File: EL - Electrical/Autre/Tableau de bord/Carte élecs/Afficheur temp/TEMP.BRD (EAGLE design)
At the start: 82 x 40 mm, 24 parts, among them IC1 MCP23008P, IC2 MCP23008P, X1 22-23-2041

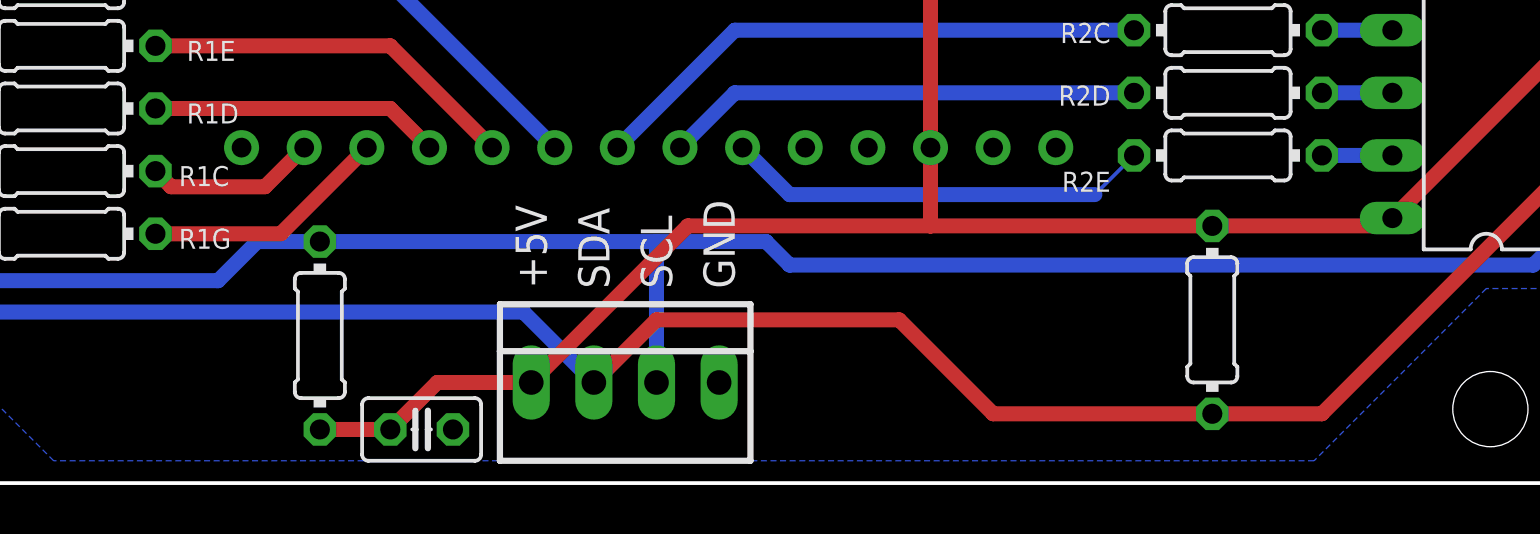
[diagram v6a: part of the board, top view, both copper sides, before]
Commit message: ajout listes composants
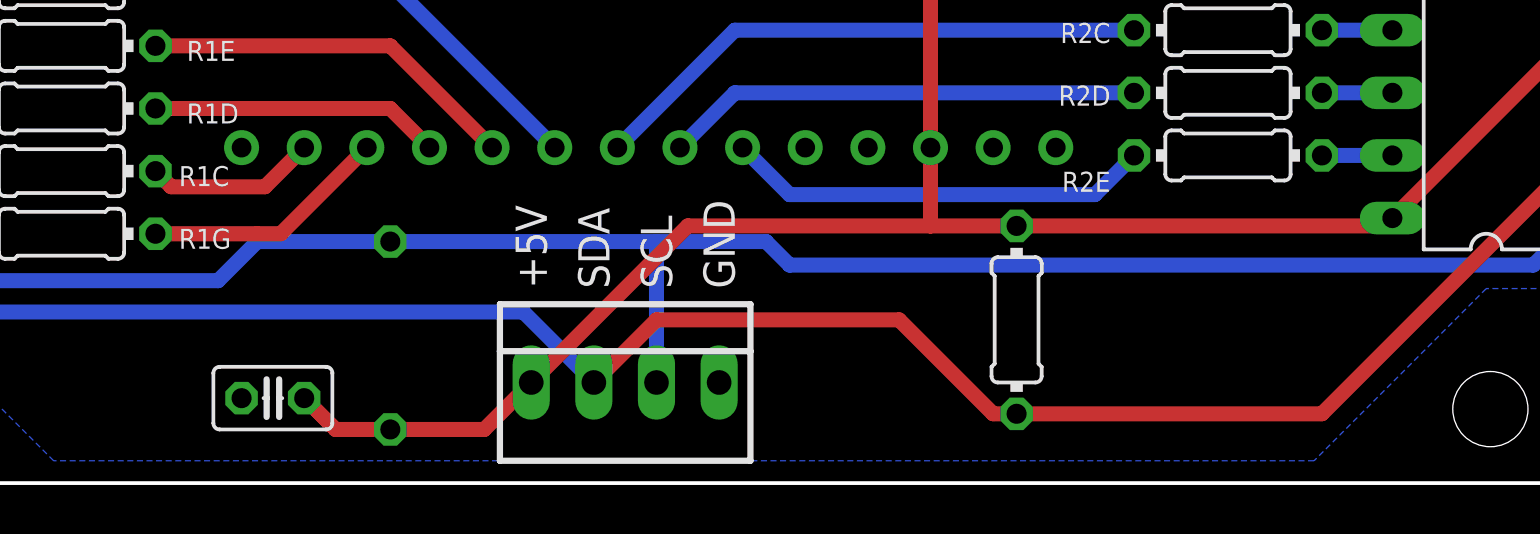
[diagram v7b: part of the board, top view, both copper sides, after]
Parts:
- moved R2 7.94 mm to (57.8, 7.62)
- moved C1 6.16 mm to (27.6, 4.45), turned to 180 degrees
- moved R1 2.86 mm to (32.4, 6.99), flipped to the bottom
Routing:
- net +5V: track 142.5 -> 143.7 mm
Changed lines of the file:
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@@
 </autorouter>
 <elements>
-<element name="C1" library="rcl" library_urn="urn:adsk.eagle:library:334" package="C025-025X050" package3d_urn="urn:adsk.eagle:package:23629/2" value="500pF" x="33.655" y="3.175" smashed="yes">
-<attribute name="SPICEPREFIX" value="C" x="33.655" y="3.175" size="1.778" layer="27" display="off"/>
-<attribute name="VALUE" x="31.369" y="4.826" size="1.27" layer="27" ratio="10"/>
+<element name="C1" library="rcl" library_urn="urn:adsk.eagle:library:334" package="C025-025X050" package3d_urn="urn:adsk.eagle:package:23629/2" value="500pF" x="27.6225" y="4.445" smashed="yes" rot="R180">
+<attribute name="SPICEPREFIX" value="C" x="27.6225" y="4.445" size="1.778" layer="27" rot="R180" display="off"/>
+<attribute name="VALUE" x="29.9085" y="7.5565" size="1.27" layer="27" ratio="10" rot="R180"/>
 </element>
 <element name="IC1" library="microchip-dspic" package="DIL18" value="MCP23008P" x="76.835" y="21.9075" smashed="yes" rot="R90">
 <attribute name="VALUE" x="77.724" y="11.7475" size="1.778" layer="27" ratio="10" rot="R90"/>
 </element>
-<element name="R1" library="rcl" library_urn="urn:adsk.eagle:library:334" package="0204/7" package3d_urn="urn:adsk.eagle:package:23498/1" value="1k" x="29.5275" y="6.985" smashed="yes" rot="R270">
-<attribute name="SPICEPREFIX" value="R" x="29.5275" y="6.985" size="1.778" layer="27" rot="R270" display="off"/>
-<attribute name="VALUE" x="29.0449" y="8.6106" size="0.9906" layer="27" ratio="10" rot="R270"/>
-</element>
-<element name="R2" library="rcl" library_urn="urn:adsk.eagle:library:334" package="0204/7" package3d_urn="urn:adsk.eagle:package:23498/1" value="1k" x="65.7225" y="7.62" smashed="yes" rot="R270">
-<attribute name="SPICEPREFIX" value="R" x="65.7225" y="7.62" size="1.778" layer="27" rot="R270" display="off"/>
-<attribute name="VALUE" x="65.2399" y="9.2456" size="0.9906" layer="27" ratio="10" rot="R270"/>
+<element name="R1" library="rcl" library_urn="urn:adsk.eagle:library:334" package="0204/7" package3d_urn="urn:adsk.eagle:package:23498/1" value="1k" x="32.385" y="6.985" smashed="yes" rot="MR270">
+<attribute name="SPICEPREFIX" value="R" x="32.385" y="6.985" size="1.778" layer="28" rot="MR270" display="off"/>
+<attribute name="VALUE" x="32.8676" y="8.6106" size="0.9906" layer="28" ratio="10" rot="MR270"/>
+</element>
+<element name="R2" library="rcl" library_urn="urn:adsk.eagle:library:334" package="0204/7" package3d_urn="urn:adsk.eagle:package:23498/1" value="1k" x="57.785" y="7.62" smashed="yes" rot="R270">
+<attribute name="SPICEPREFIX" value="R" x="57.785" y="7.62" size="1.778" layer="27" rot="R270" display="off"/>
+<attribute name="VALUE" x="57.3024" y="9.2456" size="0.9906" layer="27" ratio="10" rot="R270"/>
 </element>
 <element name="X1" library="con-molex" library_urn="urn:adsk.eagle:library:165" package="22-23-2041" value="22-23-2041" x="41.91" y="5.08" smashed="yes">
@@
 <contactref element="LED2" pad="3"/>
 <contactref element="LED2" pad="26"/>
-<wire x1="54.2925" y1="11.43" x2="65.7225" y2="11.43" width="0.6096" layer="1"/>
-<wire x1="65.7225" y1="11.43" x2="72.7075" y2="11.43" width="0.6096" layer="1"/>
+<wire x1="54.2925" y1="11.43" x2="57.785" y2="11.43" width="0.6096" layer="1"/>
 <wire x1="72.7075" y1="11.43" x2="73.025" y2="11.7475" width="0.6096" layer="1"/>
+<wire x1="72.7075" y1="11.43" x2="57.785" y2="11.43" width="0.6096" layer="1"/>
 <wire x1="38.1" y1="5.08" x2="44.45" y2="11.43" width="0.6096" layer="1"/>
 <wire x1="44.45" y1="11.43" x2="54.2925" y2="11.43" width="0.6096" layer="1"/>
@@
 <wire x1="54.2925" y1="27.6225" x2="54.2925" y2="14.605" width="0.6096" layer="1"/>
 <wire x1="38.735" y1="27.6225" x2="54.2925" y2="27.6225" width="0.6096" layer="1"/>
-<wire x1="34.29" y1="5.08" x2="32.385" y2="3.175" width="0.6096" layer="1"/>
-<wire x1="38.1" y1="5.08" x2="34.29" y2="5.08" width="0.6096" layer="1"/>
-<wire x1="29.5275" y1="3.175" x2="32.385" y2="3.175" width="0.6096" layer="1"/>
+<wire x1="38.1" y1="5.08" x2="36.195" y2="3.175" width="0.6096" layer="1"/>
+<wire x1="36.195" y1="3.175" x2="32.385" y2="3.175" width="0.6096" layer="1"/>
+<wire x1="30.1625" y1="3.175" x2="28.8925" y2="4.445" width="0.6096" layer="1"/>
+<wire x1="32.385" y1="3.175" x2="30.1625" y2="3.175" width="0.6096" layer="1"/>
 </signal>
 <signal name="SCL">
@@
 <contactref element="R1" pad="1"/>
 <contactref element="X1" pad="3"/>
-<wire x1="29.5275" y1="10.795" x2="26.9875" y2="10.795" width="0.6096" layer="16"/>
-<wire x1="26.9875" y1="10.795" x2="25.4" y2="9.2075" width="0.6096" layer="16"/>
+<wire x1="25.4" y1="9.2075" x2="26.9875" y2="10.795" width="0.6096" layer="16"/>
 <wire x1="25.4" y1="9.2075" x2="11.7475" y2="9.2075" width="0.6096" layer="16"/>
 <wire x1="10.4775" y1="10.4775" x2="10.4775" y2="27.6225" width="0.6096" layer="16"/>
@@
 <wire x1="11.7475" y1="9.2075" x2="10.4775" y2="10.4775" width="0.6096" layer="16"/>
 <wire x1="47.625" y1="10.795" x2="48.5775" y2="9.8425" width="0.6096" layer="16"/>
-<wire x1="29.5275" y1="10.795" x2="43.18" y2="10.795" width="0.6096" layer="16"/>
 <wire x1="43.18" y1="10.795" x2="47.625" y2="10.795" width="0.6096" layer="16"/>
 <wire x1="43.18" y1="5.08" x2="43.18" y2="10.795" width="0.6096" layer="16"/>
 <wire x1="48.5775" y1="9.8425" x2="78.74" y2="9.8425" width="0.6096" layer="16"/>
 <wire x1="78.74" y1="9.8425" x2="80.645" y2="11.7475" width="0.6096" layer="16"/>
+<wire x1="26.9875" y1="10.795" x2="32.385" y2="10.795" width="0.6096" layer="16"/>
+<wire x1="32.385" y1="10.795" x2="43.18" y2="10.795" width="0.6096" layer="16"/>
 </signal>
 <signal name="SDA">
@@
 <wire x1="5.715" y1="28.8925" x2="5.3975" y2="28.8925" width="0.6096" layer="16"/>
 <wire x1="37.7825" y1="7.9375" x2="10.16" y2="7.9375" width="0.6096" layer="16"/>
-<wire x1="65.7225" y1="3.81" x2="70.1675" y2="3.81" width="0.6096" layer="1"/>
+<wire x1="57.785" y1="3.81" x2="70.1675" y2="3.81" width="0.6096" layer="1"/>
 <wire x1="70.1675" y1="3.81" x2="80.645" y2="14.2875" width="0.6096" layer="1"/>
-<wire x1="56.8325" y1="3.81" x2="65.7225" y2="3.81" width="0.6096" layer="1"/>
+<wire x1="56.8325" y1="3.81" x2="57.785" y2="3.81" width="0.6096" layer="1"/>
 <wire x1="43.18" y1="7.62" x2="53.0225" y2="7.62" width="0.6096" layer="1"/>
 <wire x1="53.0225" y1="7.62" x2="56.8325" y2="3.81" width="0.6096" layer="1"/>
@@
 <contactref element="R1G" pad="1"/>
 <contactref element="LED2" pad="12"/>
-<wire x1="22.86" y1="11.1125" x2="27.94" y2="11.1125" width="0.6096" layer="1"/>
+<wire x1="22.86" y1="11.1125" x2="26.9875" y2="11.1125" width="0.6096" layer="1"/>
+<wire x1="26.9875" y1="11.1125" x2="27.94" y2="11.1125" width="0.6096" layer="1"/>
 <wire x1="27.94" y1="11.1125" x2="31.4325" y2="14.605" width="0.6096" layer="1"/>
 </signal>
@@
 <contactref element="R2E" pad="1"/>
 <contactref element="LED2" pad="6"/>
-<wire x1="62.5475" y1="14.2875" x2="60.96" y2="12.7" width="0.1524" layer="16"/>
-<wire x1="60.96" y1="12.7" x2="48.5775" y2="12.7" width="0.6096" layer="16"/>
+<wire x1="62.5475" y1="14.2875" x2="60.96" y2="12.7" width="0.6096" layer="16"/>
+<wire x1="48.5775" y1="12.7" x2="60.96" y2="12.7" width="0.6096" layer="16"/>
 <wire x1="46.6725" y1="14.605" x2="48.5775" y2="12.7" width="0.6096" layer="16"/>
+<wire x1="60.96" y1="12.7" x2="60.96" y2="12.7" width="0.6096" layer="16"/>
 </signal>
 <signal name="N$13">
